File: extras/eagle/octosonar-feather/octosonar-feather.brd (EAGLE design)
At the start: 64.8 x 22.9 mm, 39 parts, among them IC1 PCF8574TW, U1 74HC125, U2 74HC125

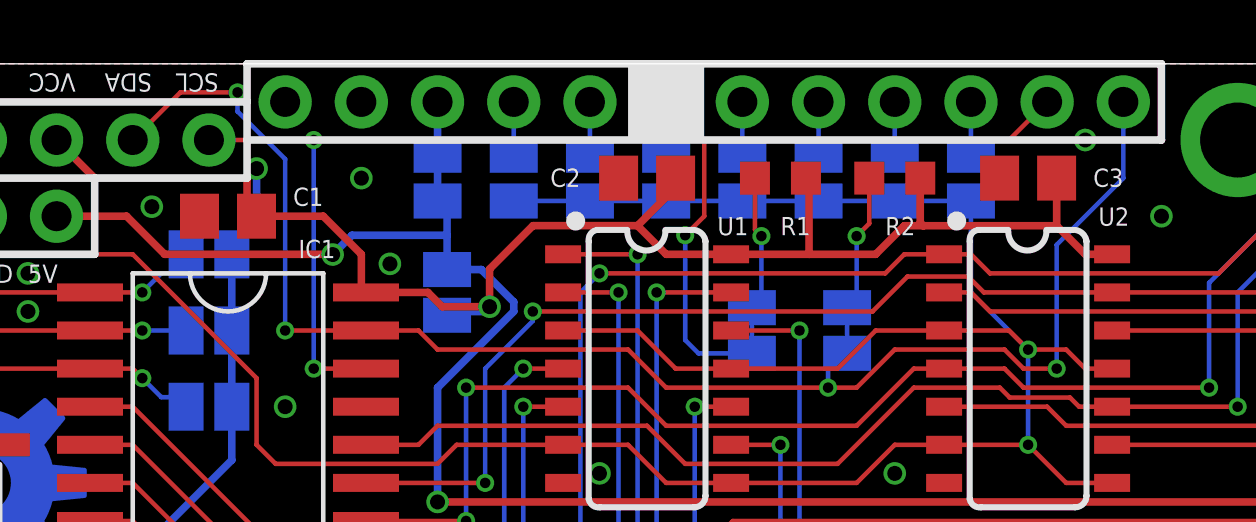
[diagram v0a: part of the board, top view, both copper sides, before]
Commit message: Changed caps to correct footprint
They were 0804 should be 0603. I changed to 0603 0.1uF a long time ago.
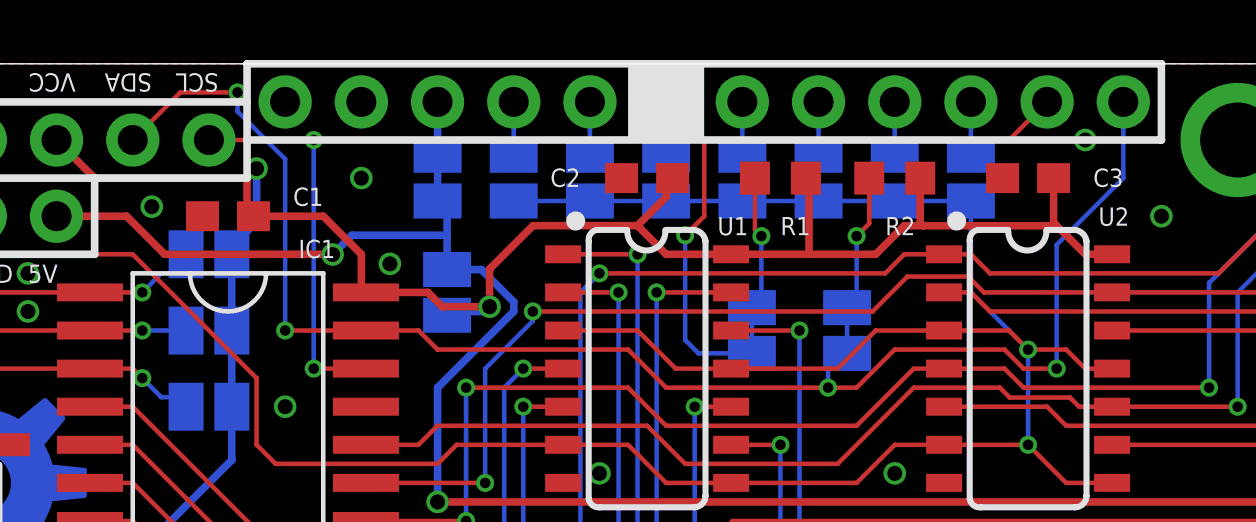
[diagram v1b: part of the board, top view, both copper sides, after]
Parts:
- C1, C2, C3: device resistor:C0805 -> rcl:C0603
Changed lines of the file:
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@@
 <attribute name="VALUE" x="14.3701" y="11.43" size="0.02" layer="28" rot="MR180"/>
 </element>
-<element name="C1" library="resistor" package="C0805" value="0.1uf" x="14.605" y="17.78" smashed="yes" rot="R180">
+<element name="C1" library="rcl" library_urn="urn:adsk.eagle:library:334" package="C0603" package3d_urn="urn:adsk.eagle:package:23616/2" value="0.1uf" x="14.605" y="17.78" smashed="yes" rot="R180">
 <attribute name="NAME" x="17.78" y="18.7325" size="0.6096" layer="25" font="vector" rot="R180"/>
+<attribute name="POPULARITY" value="37" x="14.605" y="17.78" size="1.778" layer="27" rot="R180" display="off"/>
+<attribute name="SPICEPREFIX" value="C" x="14.605" y="17.78" size="1.778" layer="27" rot="R180" display="off"/>
 <attribute name="VALUE" x="15.875" y="20.32" size="1.27" layer="27" rot="R180"/>
 </element>
-<element name="C2" library="resistor" package="C0805" value="0.1uf" x="28.575" y="19.05" smashed="yes" rot="R180">
+<element name="C2" library="rcl" library_urn="urn:adsk.eagle:library:334" package="C0603" package3d_urn="urn:adsk.eagle:package:23616/2" value="0.1uf" x="28.575" y="19.05" smashed="yes" rot="R180">
 <attribute name="NAME" x="26.3525" y="19.3675" size="0.6096" layer="25" font="vector" ratio="12" rot="R180"/>
+<attribute name="POPULARITY" value="37" x="28.575" y="19.05" size="1.778" layer="27" rot="R180" display="off"/>
+<attribute name="SPICEPREFIX" value="C" x="28.575" y="19.05" size="1.778" layer="27" rot="R180" display="off"/>
 <attribute name="VALUE" x="29.845" y="21.59" size="1.27" layer="27" rot="R180"/>
 </element>
-<element name="C3" library="resistor" package="C0805" value="0.1uf" x="41.275" y="19.05" smashed="yes" rot="R180">
+<element name="C3" library="rcl" library_urn="urn:adsk.eagle:library:334" package="C0603" package3d_urn="urn:adsk.eagle:package:23616/2" value="0.1uf" x="41.275" y="19.05" smashed="yes" rot="R180">
 <attribute name="NAME" x="44.45" y="19.3675" size="0.6096" layer="25" font="vector" ratio="12" rot="R180"/>
+<attribute name="POPULARITY" value="37" x="41.275" y="19.05" size="1.778" layer="27" rot="R180" display="off"/>
+<attribute name="SPICEPREFIX" value="C" x="41.275" y="19.05" size="1.778" layer="27" rot="R180" display="off"/>
 <attribute name="VALUE" x="42.545" y="21.59" size="1.27" layer="27" rot="R180"/>
 </element>
@@
 <wire x1="14.732" y1="13.97" x2="14.732" y2="16.51" width="0.254" layer="16"/>
 <contactref element="IC1" pad="16"/>
-<wire x1="29.525" y1="19.05" x2="29.525" y2="18.7325" width="0.254" layer="1"/>
-<wire x1="29.525" y1="18.7325" x2="28.25625" y2="17.46375" width="0.254" layer="1"/>
-<wire x1="28.255" y1="17.465" x2="28.25625" y2="17.46375" width="0.254" layer="1"/>
-<wire x1="28.25625" y1="17.46375" x2="29.21" y2="16.51" width="0.254" layer="1"/>
+<wire x1="28.255" y1="17.465" x2="29.21" y2="16.51" width="0.254" layer="1"/>
 <wire x1="29.21" y1="16.51" x2="31.375" y2="16.51" width="0.254" layer="1"/>
-<wire x1="42.225" y1="19.05" x2="42.2275" y2="19.0475" width="0.1524" layer="1"/>
-<wire x1="42.2275" y1="19.0475" x2="42.2275" y2="17.4625" width="0.254" layer="1"/>
 <wire x1="42.2275" y1="17.4625" x2="43.18" y2="16.51" width="0.254" layer="1"/>
 <wire x1="43.18" y1="16.51" x2="44.075" y2="16.51" width="0.254" layer="1"/>
@@
 <wire x1="8.89" y1="20.32" x2="10.16" y2="19.05" width="0.254" layer="1"/>
 <wire x1="24.7715" y1="17.465" x2="28.255" y2="17.465" width="0.254" layer="1"/>
-<wire x1="31.375" y1="16.51" x2="33.9725" y2="16.51" width="0.254" layer="1"/>
-<wire x1="33.9725" y1="16.51" x2="36.195" y2="16.51" width="0.254" layer="1"/>
-<wire x1="36.195" y1="16.51" x2="37.1475" y2="17.4625" width="0.254" layer="1"/>
+<wire x1="37.1475" y1="17.4625" x2="36.195" y2="16.51" width="0.254" layer="1"/>
 <wire x1="37.1475" y1="17.4625" x2="37.7825" y2="17.4625" width="0.254" layer="1"/>
 <wire x1="37.7825" y1="17.4625" x2="42.2275" y2="17.4625" width="0.254" layer="1"/>
-<wire x1="33.87" y1="19.05" x2="33.9725" y2="18.9475" width="0.254" layer="1"/>
 <wire x1="37.68" y1="19.05" x2="37.68" y2="17.565" width="0.254" layer="1"/>
 <wire x1="37.68" y1="17.565" x2="37.7825" y2="17.4625" width="0.254" layer="1"/>
-<wire x1="33.9725" y1="18.9475" x2="33.9725" y2="16.51" width="0.254" layer="1"/>
 <wire x1="14.605" y1="16.637" x2="14.732" y2="16.51" width="0.254" layer="16"/>
 <contactref element="MS1" pad="2"/>
@@
 <wire x1="23.3245375" y1="16.0180375" x2="23.3245375" y2="14.76375" width="0.254" layer="1"/>
 <wire x1="15.24" y1="19.05" x2="15.24" y2="18.095" width="0.254" layer="1"/>
-<wire x1="15.24" y1="18.095" x2="15.555" y2="17.78" width="0.254" layer="1"/>
+<wire x1="15.24" y1="18.095" x2="15.455" y2="17.78" width="0.254" layer="1"/>
 <wire x1="15.24" y1="19.05" x2="15.5575" y2="19.3675" width="0.254" layer="1"/>
-<wire x1="15.555" y1="17.78" x2="17.78" y2="17.78" width="0.254" layer="1"/>
+<wire x1="15.455" y1="17.78" x2="17.78" y2="17.78" width="0.254" layer="1"/>
 <wire x1="17.78" y1="17.78" x2="19.05" y2="16.51" width="0.254" layer="1"/>
 <wire x1="19.05" y1="16.51" x2="19.05" y2="15.24" width="0.254" layer="1"/>
 <wire x1="19.05" y1="15.24" x2="19.205" y2="15.24" width="0.254" layer="1"/>
+<wire x1="36.195" y1="16.51" x2="33.9725" y2="16.51" width="0.254" layer="1"/>
+<wire x1="33.9725" y1="16.51" x2="31.375" y2="16.51" width="0.254" layer="1"/>
+<wire x1="33.87" y1="19.05" x2="33.9725" y2="18.9475" width="0.254" layer="1"/>
+<wire x1="33.9725" y1="18.9475" x2="33.9725" y2="16.51" width="0.254" layer="1"/>
+<wire x1="28.255" y1="17.465" x2="29.205" y2="18.415" width="0.254" layer="1"/>
+<wire x1="29.21" y1="18.415" x2="29.205" y2="18.415" width="0.254" layer="1"/>
+<wire x1="42.2275" y1="17.4625" x2="42.125" y2="17.565" width="0.254" layer="1"/>
+<wire x1="42.125" y1="17.565" x2="42.125" y2="19.05" width="0.254" layer="1"/>
+<wire x1="29.425" y1="19.05" x2="29.21" y2="18.835" width="0.254" layer="1"/>
+<wire x1="29.21" y1="18.835" x2="29.21" y2="18.415" width="0.254" layer="1"/>
 </signal>
 <signal name="P0">

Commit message: Octosonar v3.0.0 prod featherwing design
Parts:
- A0, A1, A2, JP1, JP2, JP3, JP4, JP5, JP6, JP7, JP8, JP9, V1, V2: device jumper:SJ -> redhunter:SJ-NOCREAM
- moved J2 2.54 mm to (6.35, 17.8), turned to 0 degrees
- renumbered S0 to 0, S1 to 1, S2 to 2, S3 to 3, S4 to 4, S5 to 5, S6 to 6, S7 to 7
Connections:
- net 5V renamed VS
- net GND: no longer J2.2
- net INT: now also J2.2
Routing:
- net VS: track 95.6 -> 99.2 mm
- net INT: track 93.6 -> 94.9 mm
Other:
- board text added: "Cut V2 to disconnect VS line for HC-SR04 power from FeatherWing USB pin. YOU MUST DO THIS IF CONNECTING V1"
- board text added: "INT"
- board text added: "OctoSonar "FeatherWing""
- board text added: "Solder V1 to connect VCC to VS lines for HC-SR04 power. ONLY DO THIS IF VCC AND VS ARE THE SAME"
- board text added: "V3.0.0"
- board text added: "VS"
- board text removed: "5V"
- board text removed: "Cut V2 to disconnect 5V lines for HC-SR04 power from FeatherWing USB pin. You may want this if you are using an external 5V supply."
- board text removed: "OctoSonar - FeatherWing"
- board text removed: "Solder V1 to connect VCC to 5V lines for HC-SR04 power. DO NOT DO THIS ON 3V CONTROLLERS OR FEATHER PROJECTS"
- board text removed: "V0.0.2"
